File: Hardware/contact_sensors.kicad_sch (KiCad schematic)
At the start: 26 parts, among them J16 DG250-3-5-02P-11-00AH, J17 DG250-3-5-02P-11-00AH, J18 DG250-3-5-02P-11-00AH, J19 DG250-3-5-02P-11-00AH, J20 DG250-3-5-02P-11-00AH, J21 DG250-3-5-02P-11-00AH, J22 DG250-3-5-02P-11-00AH, J23 DG250-3-5-02P-11-00AH, U15 LTV-847S, U16 LTV-847S

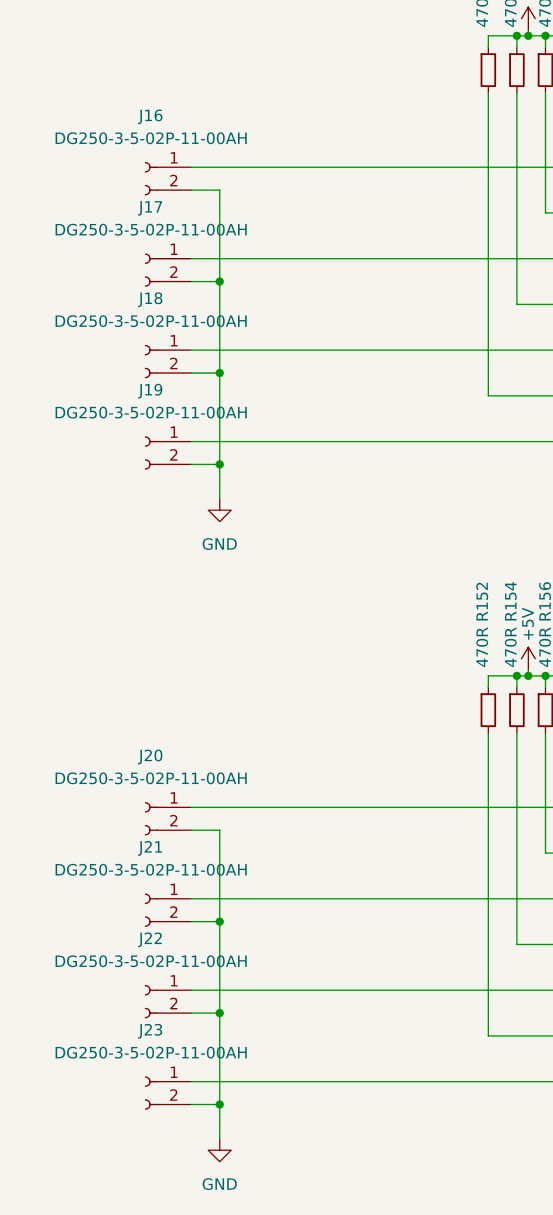
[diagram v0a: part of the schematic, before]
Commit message: Toolchain set. Timer module added. Schematic files migrated.
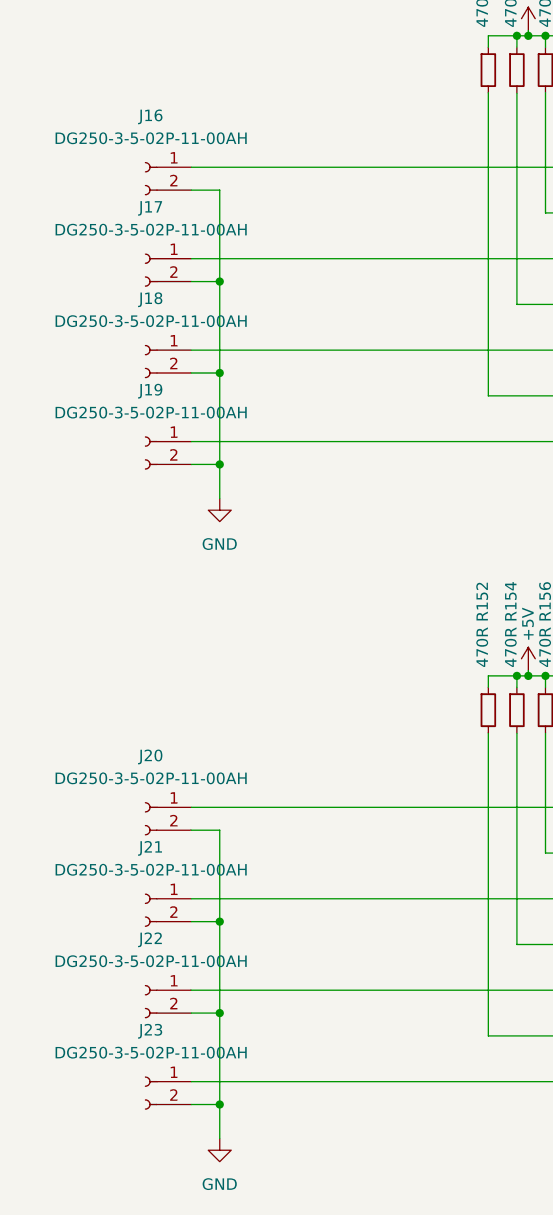
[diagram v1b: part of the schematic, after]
